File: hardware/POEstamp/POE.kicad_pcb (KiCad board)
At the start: 2 copper layers, 70 x 40 mm, 61 parts, among them J1 0813-1X1T-57-F, P3 GND, P4 +5V, P5 CONN_01X05, P6 5Vout, P7 GNDout, Q1 SI3440DV, NFET, Q2 2N7002, Q3 MMBTA42, T1 PA1134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

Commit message: Fixed backwards LED and finished putting all components within the board outline. Everything should be close to its final location, all silk screens are aligned pretty alright.
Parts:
- removed REF**11, REF**12, REF**21, REF**22: MountingHole_3-5mm, Mounting_Holes:MountingHole_3-5mm
- added REF**: MountingHole_3-5mm, Mounting_Holes:MountingHole_3-5mm, F.Cu at (75.0, 39.0)
- added REF**: MountingHole_3-5mm, Mounting_Holes:MountingHole_3-5mm, F.Cu at (75.0, 69.0)
- added REF**: MountingHole_3-5mm, Mounting_Holes:MountingHole_3-5mm, F.Cu at (135.0, 69.0)
- added REF**: MountingHole_3-5mm, Mounting_Holes:MountingHole_3-5mm, F.Cu at (135.0, 39.0)
- moved D12 33.8 mm to (138.2, 44.5)
- moved R22 31.8 mm to (138.2, 47.8), turned to 90 degrees
- moved C15 21.7 mm to (131.2, 46.0), turned to 0 degrees
- moved C14 20.6 mm to (131.2, 43.8), turned to 0 degrees
- moved R3 5.46 mm to (101.2, 54.5), turned to 0 degrees
- moved R5 3.87 mm to (107.5, 57.0), turned to 90 degrees
- moved P6 3.75 mm to (125.0, 37.0)
- moved P7 3.51 mm to (119.5, 36.8)
- moved C9 3.25 mm to (122.5, 43.2)
- moved D7 2.06 mm to (110.2, 67.5)
- moved Q2 2.00 mm to (110.2, 64.0)
- moved R21 1.77 mm to (129.5, 70.8)
- moved C12 1.46 mm to (124.2, 72.2)
- moved C13 1.46 mm to (124.2, 69.1)
- moved R11 1.46 mm to (124.2, 70.8)
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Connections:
- D12 pad 1: Net-(D12-Pad1) -> GND
- D12 pad 2: GND -> Net-(D12-Pad2)
- R22 pad 2: Net-(D12-Pad1) -> Net-(D12-Pad2)
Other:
- board text added: "5V"
- board text added: "GND"

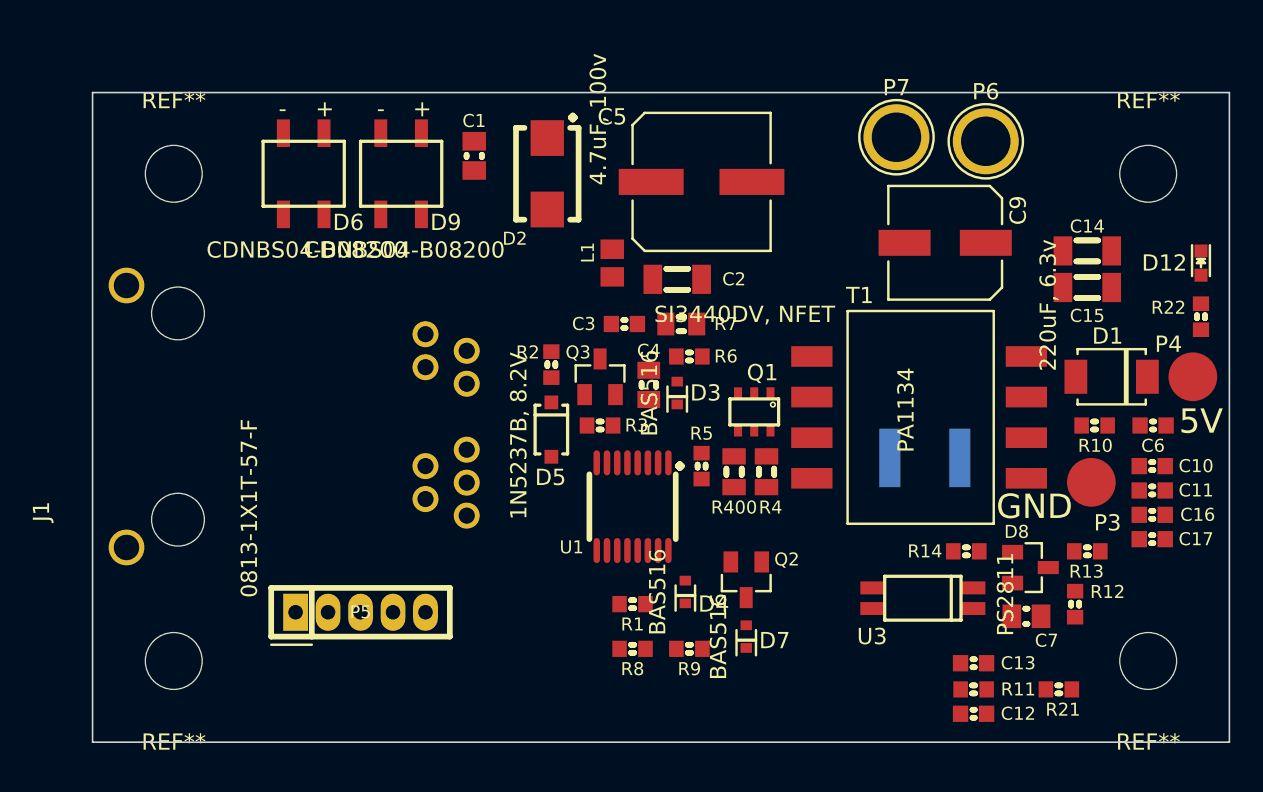
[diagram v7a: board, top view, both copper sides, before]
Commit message: Added ground zones and silkscreened the isolation path.
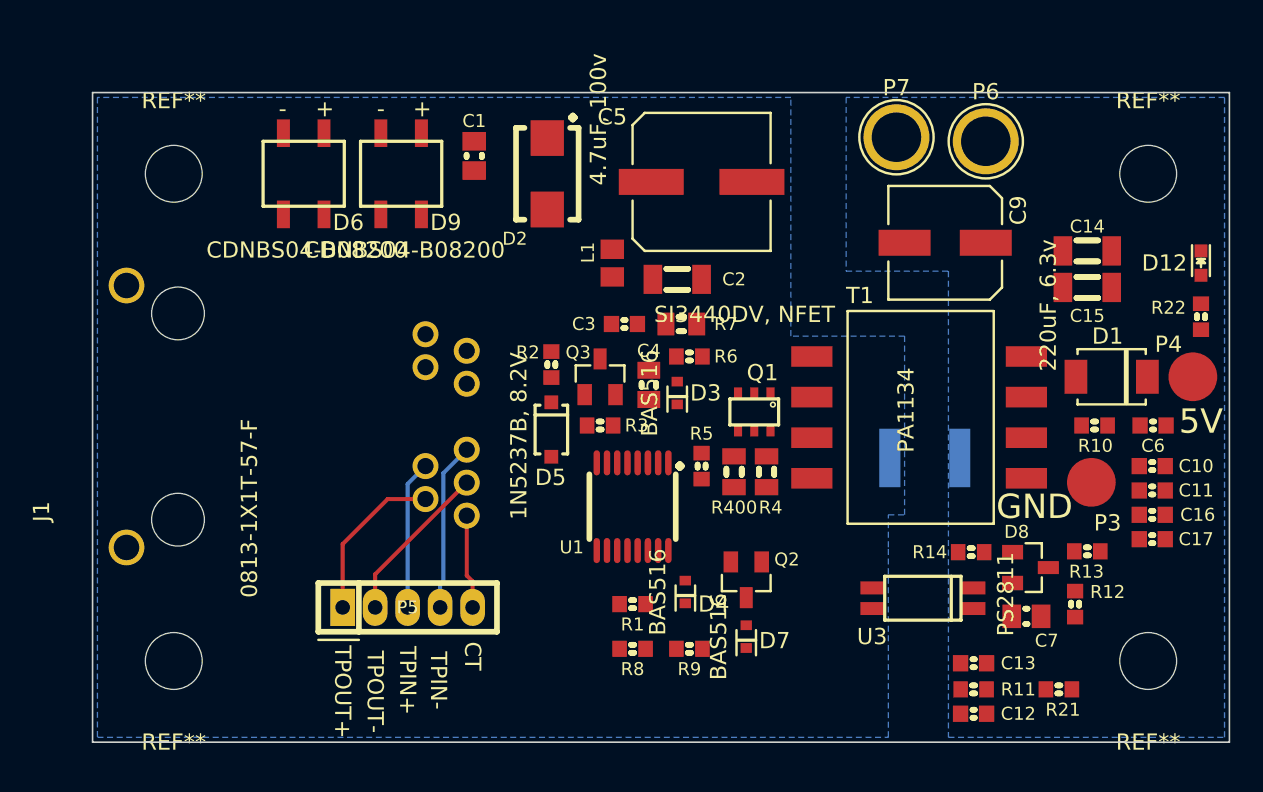
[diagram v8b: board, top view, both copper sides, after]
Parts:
- moved P5 2.92 mm to (89.4, 65.7)
- moved R14 0.30 mm to (124.1, 62.3)
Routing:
- net /TPIN-: track 0.00 -> 10.4 mm
- net /TPOUT+: track 0.00 -> 10.1 mm
- net /TPOUT-: track 0.00 -> 10.0 mm
- net /TPIN+: track 0.00 -> 9.16 mm
- net /CT: track 0.00 -> 5.80 mm
- added copper zone on B.Cu, net GND
- added copper zone on B.Cu, net GNDA
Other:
- board text added: "CT"
- board text added: "ISOLATION"
- board text added: "TPIN+"
- board text added: "TPIN-"
- board text added: "TPOUT+"
- board text added: "TPOUT-"
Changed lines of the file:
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@@
     (area 69.949999 33.949999 140.050001 74.050001)
     (thickness 1.6)
-    (drawings 10)
-    (tracks 0)
+    (drawings 22)
+    (tracks 14)
     (zones 0)
     (modules 61)
@@
   )
   (module conn-2mm:CONN-2MM-F-1x5 (layer F.Cu)
-    (at 86.5 66)
+    (at 89.4 65.7)
     (fp_text reference P5 (at 0 0) (layer F.SilkS)
       (effects (font (size 0.8 0.8) (thickness 0.15)))
@@
   )
   (module IPC7351-Nominal:RESC1608X55 (layer F.Cu)
-    (at 123.8 62.25 180)
+    (at 124.1 62.3 180)
     (descr "Resistor,Chip;1.60mm L X 0.85mm W X 0.55mm H")
     (attr smd)
@@
       (net 7 5VPoE))
   )
+  (gr_text ISOLATION (at 122.2 67.7 90) (layer B.SilkS)
+    (effects (font (size 1.5 1.5) (thickness 0.3)) (justify mirror))
+  )
+  (gr_text ISOLATION (at 116 40.7 90) (layer B.SilkS)
+    (effects (font (size 1.5 1.5) (thickness 0.3)) (justify mirror))
+  )
+  (gr_line (start 120.9 61.2) (end 120.9 73) (layer B.SilkS) (width 0.2))
+  (gr_line (start 121.3 61.2) (end 120.9 61.2) (layer B.SilkS) (width 0.2))
+  (gr_line (start 121.3 47) (end 121.3 61.2) (layer B.SilkS) (width 0.2))
+  (gr_line (start 114.6 47) (end 121.3 47) (layer B.SilkS) (width 0.2))
+  (gr_line (start 114.6 35) (end 114.6 47) (layer B.SilkS) (width 0.2))
+  (gr_text CT (at 93.4 68.7 270) (layer F.SilkS)
+    (effects (font (size 1 1) (thickness 0.25)))
+  )
+  (gr_text TPIN- (at 91.3 70.2 270) (layer F.SilkS)
+    (effects (font (size 1 1) (thickness 0.25)))
+  )
+  (gr_text TPIN+ (at 89.4 70.2 270) (layer F.SilkS)
+    (effects (font (size 1 1) (thickness 0.25)))
+  )
+  (gr_text TPOUT- (at 87.4 70.9 270) (layer F.SilkS)
+    (effects (font (size 1 1) (thickness 0.25)))
+  )
+  (gr_text TPOUT+ (at 85.4 70.9 270) (layer F.SilkS)
+    (effects (font (size 1 1) (thickness 0.25)))
+  )
   (gr_text GND (at 128 59.5) (layer F.SilkS)
     (effects (font (size 1.5 1.5) (thickness 0.3)))
@@
     (arrow2b (pts (xy 66.000098 34) (xy 66.586519 35.126504)))
   )
+  (segment (start 88.17 59.03) (end 85.4 61.8) (width 0.25) (layer F.Cu) (net 24))
+  (segment (start 85.4 61.8) (end 85.4 65.7) (width 0.25) (layer F.Cu) (net 24))
+  (segment (start 90.5 59.03) (end 88.17 59.03) (width 0.25) (layer F.Cu) (net 24))
+  (segment (start 90.5 57) (end 89.4 58.1) (width 0.25) (layer B.Cu) (net 25))
+  (segment (start 89.4 58.1) (end 89.4 65.7) (width 0.25) (layer B.Cu) (net 25))
+  (segment (start 93.04 63.74) (end 93.4 64.1) (width 0.25) (layer F.Cu) (net 26))
+  (segment (start 93.4 64.1) (end 93.4 65.7) (width 0.25) (layer F.Cu) (net 26))
+  (segment (start 93.04 60.05) (end 93.04 63.74) (width 0.25) (layer F.Cu) (net 26))
+  (segment (start 93.04 58.02) (end 87.4 63.66) (width 0.25) (layer F.Cu) (net 27))
+  (segment (start 87.4 63.66) (end 87.4 65.7) (width 0.25) (layer F.Cu) (net 27))
+  (segment (start 91.6 57.43) (end 91.6 64.107) (width 0.25) (layer B.Cu) (net 28))
+  (segment (start 91.4 64.307) (end 91.4 65.7) (width 0.25) (layer B.Cu) (net 28))
+  (segment (start 91.6 64.107) (end 91.4 64.307) (width 0.25) (layer B.Cu) (net 28))
+  (segment (start 93.04 55.99) (end 91.6 57.43) (width 0.25) (layer B.Cu) (net 28))
+  (zone (net 4) (net_name GNDA) (layer B.Cu) (hatch edge 0.508)
+    (connect_pads yes (clearance 0.15))
+    (min_thickness 0.15)
+    (fill yes (arc_segments 16) (thermal_gap 0.508) (thermal_bridge_width 0.508))
+    (polygon
+      (pts
+        (xy 70.3 34.3) (xy 70.3 73.7) (xy 119 73.7) (xy 119 62) (xy 119 60)
+        (xy 120 60) (xy 120 49) (xy 113 49) (xy 113 34.3)
+      )
+    )
+  )
+  (zone (net 11) (net_name GND) (layer B.Cu) (hatch edge 0.508)
+    (connect_pads yes (clearance 0.15))
+    (min_thickness 0.15)
+    (fill yes (mode segment) (arc_segments 16) (thermal_gap 0.508) (thermal_bridge_width 0.508))
+    (polygon
+      (pts
+        (xy 116.4 34.3) (xy 116.4 45) (xy 122.7 45) (xy 122.7 73.7) (xy 139.7 73.7)
+        (xy 139.7 34.3)
+      )
+    )
+  )
 )
